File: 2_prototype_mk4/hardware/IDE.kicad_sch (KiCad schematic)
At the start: 4 parts, among them J3 Conn_02x20_Odd_Even, J4 1734451-1

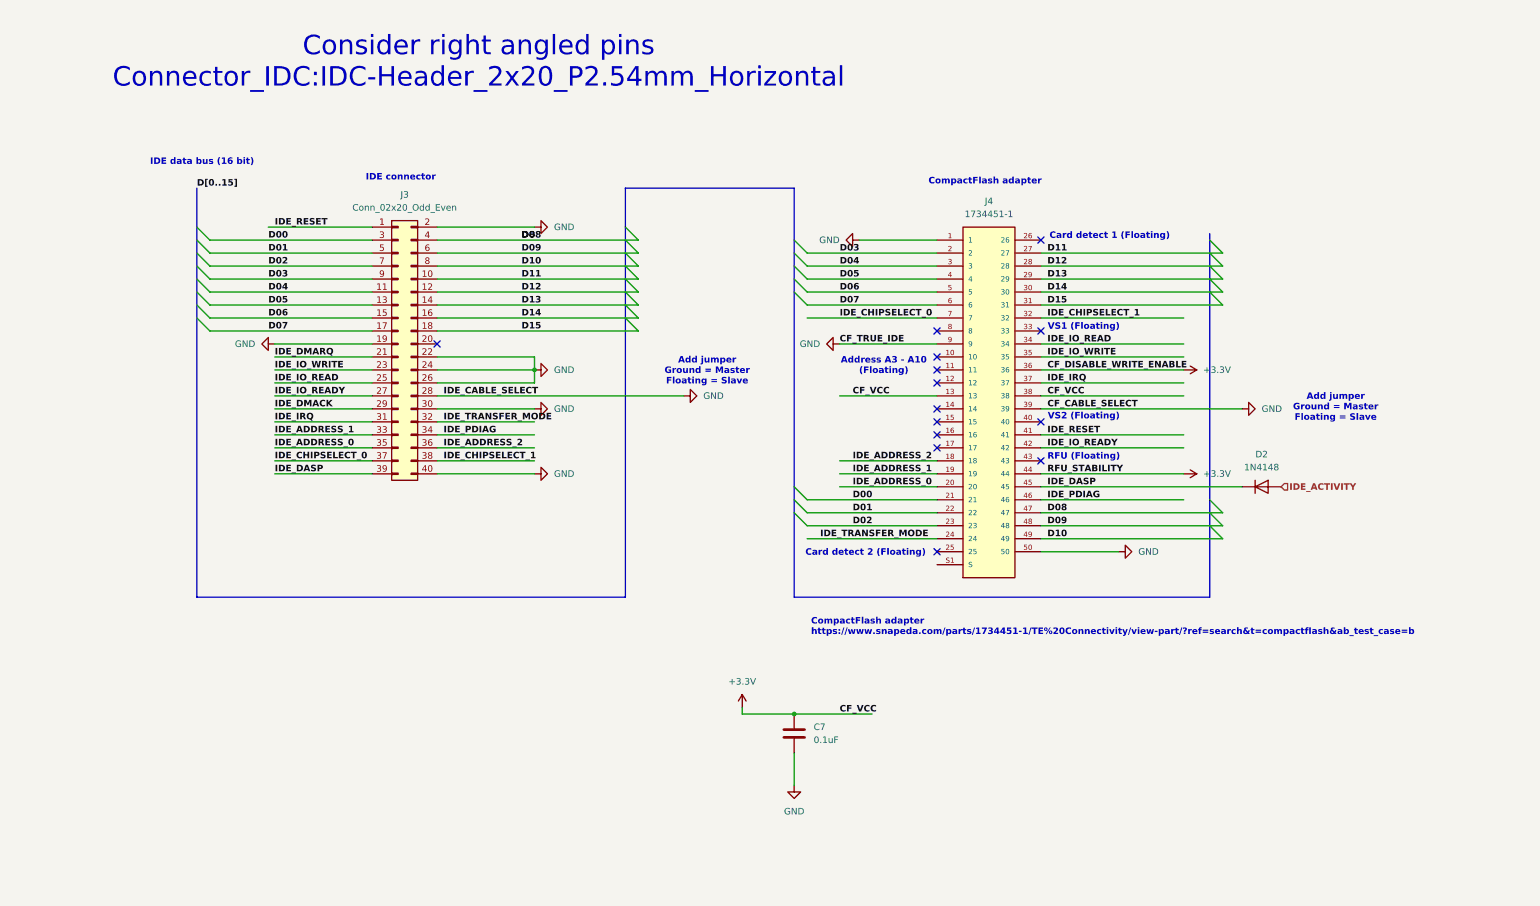
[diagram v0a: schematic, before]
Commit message: Create initial MK4 PCB layout
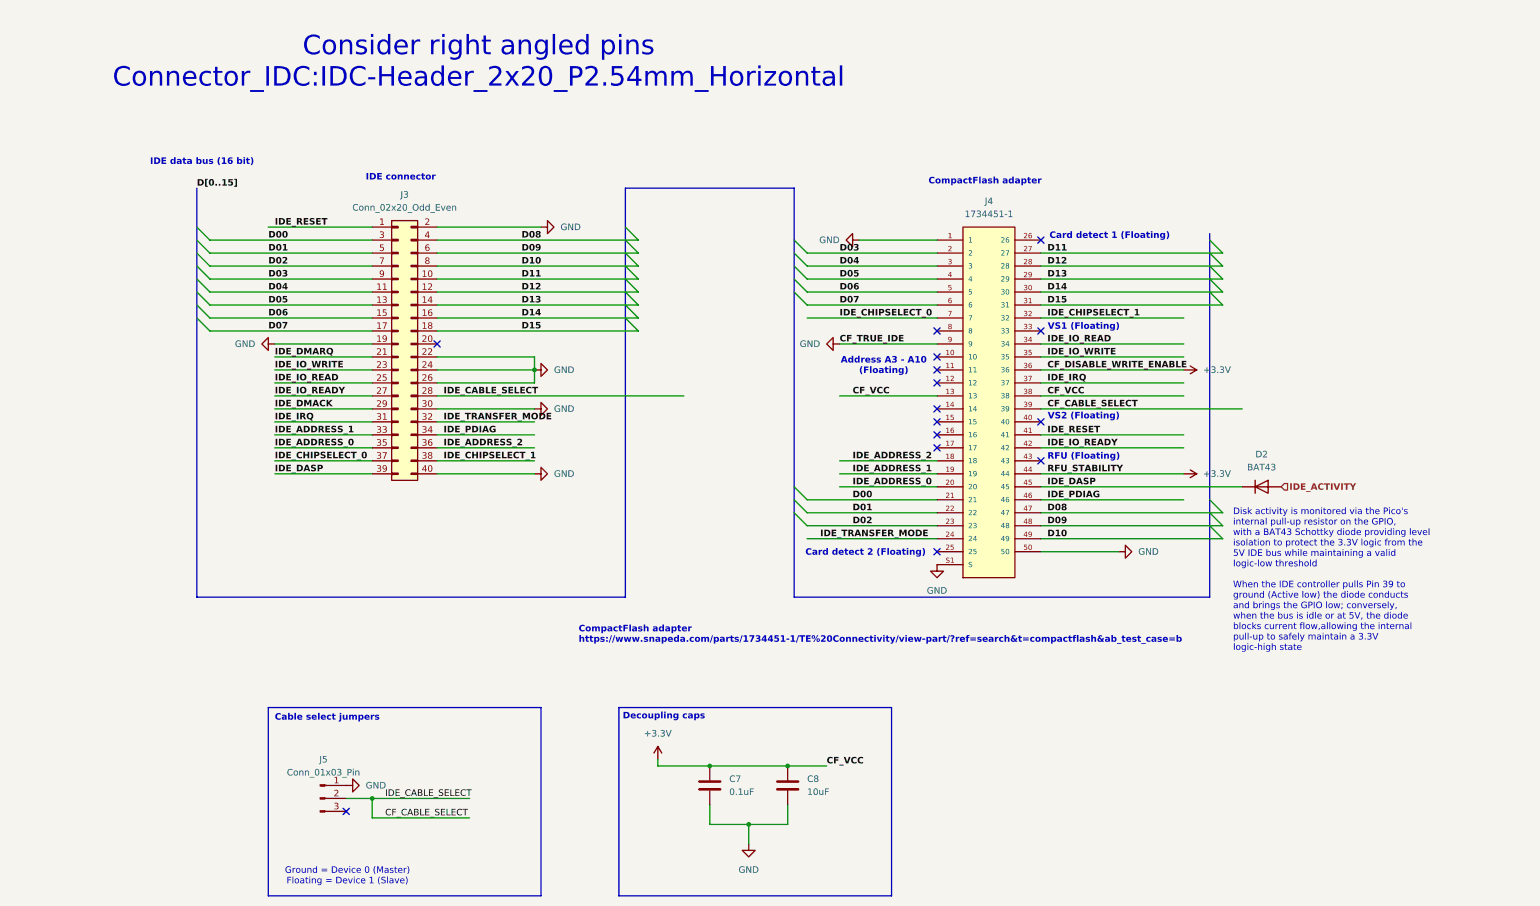
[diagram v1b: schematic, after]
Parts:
- added C8: 10uF, Capacitor_SMD:C_1206_3216Metric, symbol Device:C
- added J5: Conn_01x03_Pin, Connector_PinHeader_2.54mm:PinHeader_1x03_P2.54mm_Vertical, symbol Connector:Conn_01x03_Pin
- D2: value 1N4148 -> BAT43; footprint Diode_THT:D_DO-35_SOD27_P7.62mm_Horizontal -> Diode_SMD:D_SOD-123
- J4: footprint 1734451-1:TE_1734451-1 -> Custom:TE_1734451-1
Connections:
- net +3.3V: now also C8.1
- net GND: now also J4.S1 (S), J4.S2 (S), C8.2, J5.1 (Pin_1); no longer J3.28 (Pin_28), J4.39
- new net CF_CABLE_SELECT: J3.28 (Pin_28), J4.39, J5.2 (Pin_2)
- no-connect marks 14 -> 15
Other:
- note added: "Cable select jumpers"
- note added: "Decoupling caps"
- note added: "Disk activity is monitored via the Pico's internal pull-up resistor on the GPIO, with a BAT43 Schottky diode providing level isolation to protect the 3.3V logic from the 5V IDE bus while maintaining a valid logic-low threshold When the IDE controller pulls Pin 39 to ground (Active low) the diode conducts and brings the GPIO low; conversely, when the bus is idle or at 5V, the diode blocks current 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"
- note added: "Ground = Device 0 (Master) Floating = Device 1 (Slave)"
- note removed: "Add jumper Ground = Master Floating = Slave"
- moved on the sheet: C7

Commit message: MK4 PCB layout complete
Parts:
- added R3, R6: 10K, Resistor_SMD:R_0603_1608Metric, symbol Device:R
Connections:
- net +3.3V: now also R6.2; no longer J4.44
- net GND: now also R3.2
- net IDE_DMACK: now also J4.44, R6.1
- net IDE_DMARQ: now also J4.43, R3.1
- no-connect marks 15 -> 14
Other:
- note added: "DMA acknowledge Pull up"
- note added: "DMA request Pull down"
- note removed: "RFU (Floating)"

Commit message: Final design to sent to PCBWay
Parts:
- removed R6: 10K, Resistor_SMD:R_0603_1608Metric, symbol Device:R
- R3: value 10K -> 4.7K
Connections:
- net +3.3V: now also R3.1; no longer C7.1, C8.1, J4.13, J4.36, J4.38
- net D00: now also J3.17 (Pin_17); no longer J3.3 (Pin_3)
- net D01: now also J3.15 (Pin_15); no longer J3.5 (Pin_5)
- net D02: now also J3.13 (Pin_13); no longer J3.7 (Pin_7)
- net D03: now also J3.11 (Pin_11); no longer J3.9 (Pin_9)
- net D04: now also J3.9 (Pin_9); no longer J3.11 (Pin_11)
- net D05: now also J3.7 (Pin_7); no longer J3.13 (Pin_13)
- net D06: now also J3.5 (Pin_5); no longer J3.15 (Pin_15)
- net D07: now also J3.3 (Pin_3); no longer J3.17 (Pin_17)
- net GND: now also J4.10, J4.11, J4.12, J4.14, J4.15, J4.16, J4.17, J4.33, J4.8; no longer R3.2
- net IDE_ACTIVITY: now also R3.2
- net IDE_DMACK: no longer names the net of J3.29 (Pin_29)
- net IDE_DMACK: no longer J4.44
- removed net IDE_DMARQ: J3.21 (Pin_21), J4.43, R3.1
- new net POWER_5V_SUP: C7.1, C8.1, J4.13, J4.38, J4.44
- no-connect marks 14 -> 9
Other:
- note added: "Address A3 - A10"
- note added: "DMACK for DMA mode (unsupported currently)"
- note added: "DMARQ for DMA mode (unsupported currently)"
- note added: "IDE to CompactFlash adapter schematic from https://allpinouts.org/pinouts/cables/data_storage/ide-to-compactflash-cf-adapter-schematic/"
- note added: "Write Enable (Floating)"
- note removed: "Address A3 - A10 (Floating)"
- note removed: "DMA acknowledge Pull up"
- note removed: "DMA request Pull down"
- note removed: "VS1 (Floating)"

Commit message: Final MKIV tweaks before sending off to PCBWay
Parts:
- D2: value BAT43 -> BAT43W
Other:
- note added: "Disk activity is monitored via the Pico's internal pull-up resistor on the GPIO, with a BAT43W Schottky diode providing level isolation to protect the 3.3V logic from the 5V IDE bus while maintaining a valid logic-low threshold When the IDE controller pulls Pin 39 to ground (Active low) the diode conducts and brings the GPIO low; conversely, when the bus is idle or at 5V, the diode blocks current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"
- note removed: "Disk activity is monitored via the Pico's internal pull-up resistor on the GPIO, with a BAT43 Schottky diode providing level isolation to protect the 3.3V logic from the 5V IDE bus while maintaining a valid logic-low threshold When the IDE controller pulls Pin 39 to ground (Active low) the diode conducts and brings the GPIO low; conversely, when the bus is idle or at 5V, the diode blocks current 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"
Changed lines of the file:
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@@
 		)
 	)
-	(text "Disk activity is monitored via the Pico's \ninternal pull-up resistor on the GPIO, \nwith a BAT43 Schottky diode providing level \nisolation to protect the 3.3V logic from the \n5V IDE bus while maintaining a valid \nlogic-low threshold\n\nWhen the IDE controller pulls Pin 39 to \nground (Active low) the diode conducts \nand brings the GPIO low; conversely, \nwhen the bus is idle or at 5V, the diode \nblocks current flow,allowing the internal \npull-up to safely maintain a 3.3V \nlogic-high state"
+	(text "Disk activity is monitored via the Pico's \ninternal pull-up resistor on the GPIO, \nwith a BAT43W Schottky diode providing level \nisolation to protect the 3.3V logic from the \n5V IDE bus while maintaining a valid \nlogic-low threshold\n\nWhen the IDE controller pulls Pin 39 to \nground (Active low) the diode conducts \nand brings the GPIO low; conversely, \nwhen the bus is idle or at 5V, the diode \nblocks current flow,allowing the internal \npull-up to safely maintain a 3.3V \nlogic-high state"
 		(exclude_from_sim no)
 		(at 238.252 127.508 0)
@@
 	(wire
 		(pts
+			(xy 49.53 58.42) (xy 69.85 58.42)
+		)
+		(stroke
+			(width 0)
+			(type default)
+		)
+	)
+	(wire
+		(pts
 			(xy 50.8 88.9) (xy 69.85 88.9)
 		)
@@
 	(wire
 		(pts
-			(xy 49.53 58.42) (xy 69.85 58.42)
-		)
-		(stroke
-			(width 0)
-			(type default)
-		)
-	)
-	(wire
-		(pts
 			(xy 177.8 99.06) (xy 180.34 99.06)
 		)
@@
 	)
 	(hierarchical_label "IDE_ACTIVITY"
-		(shape input)
+		(shape output)
 		(at 260.35 109.22 0)
 		(effects
@@
 		)
 	)
+	(hierarchical_label "IDE_RESET"
+		(shape output)
+		(at 49.53 58.42 180)
+		(effects
+			(font
+				(size 1.27 1.27)
+			)
+			(justify right)
+		)
+	)
 	(netclass_flag ""
 		(length 2.54)
@@
 			)
 		)
-		(property "Datasheet" ""
+		(property "Datasheet" "https://www.snapeda.com/parts/1734451-1/TE%20Connectivity/view-part/?ref=search&t=compactflash&ab_test_case=b"
 			(at 190.5 91.44 0)
 			(hide yes)
@@
 			)
 		)
-		(property "Value" "BAT43"
+		(property "Value" "BAT43W"
 			(at 243.84 105.41 0)
 			(show_name no)
@@
 			)
 		)
-		(property "Datasheet" "https://assets.nexperia.com/documents/data-sheet/1N4148_1N4448.pdf"
+		(property "Datasheet" ""
 			(at 243.84 109.22 0)
 			(hide yes)
@@
 			)
 		)
-		(property "Datasheet" ""
+		(property "Datasheet" "https://www.lcsc.com/product-detail/C19193815.html?s_z=n_q_p_C2541WV-2X20P-A1&spm=wm.ssy.bg.13.stp&lcsc_vid=RFVXVVNXQlReBVQDFlULVl1VFgVaUlVQRFUIVgVTRlYxVlNRTlVYU11eRFhWVjsOAxUeFF5JWBYZEEoKFBINSQcJGk4dAgUUFAk%3D"
 			(at 74.93 81.28 0)
 			(hide yes)
